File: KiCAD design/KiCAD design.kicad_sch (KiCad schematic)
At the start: 3 parts, among them U101 NUCLEO64-F411RE

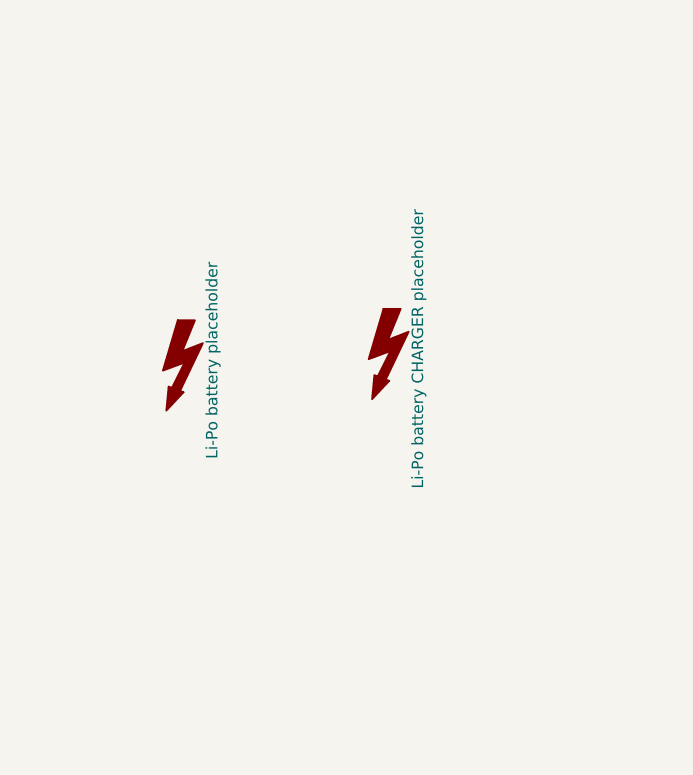
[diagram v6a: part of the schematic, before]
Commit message: added PurchaseLoc and Price to most of the main components, leds, resistors, capacitors, switch, bluetooth missing
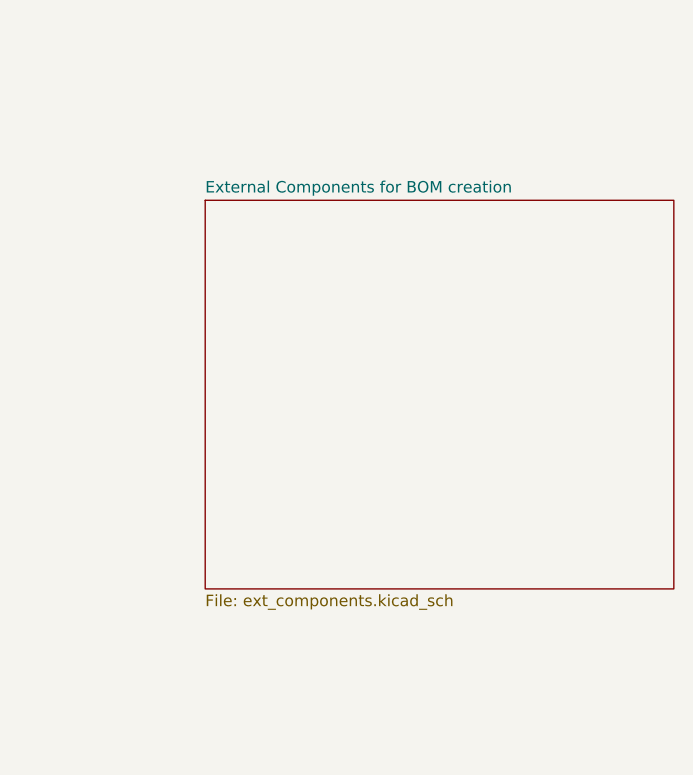
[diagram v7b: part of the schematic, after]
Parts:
- removed LiPo_bat401: Li-Po battery placeholder, symbol Graphic:SYM_Flash_Large
- removed LiPo_charger401: Li-Po battery CHARGER placeholder, symbol Graphic:SYM_Flash_Large
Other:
- added sheet External Components for BOM creation (ext_components.kicad_sch)
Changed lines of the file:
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@@
     (stroke (width 0) (type default) (color 0 0 0 0))
-  )
-  (symbol (lib_id "Graphic:SYM_Flash_Large") (at 207.01 127 0) (unit 1)
-    (in_bom yes) (on_board yes) (fields_autoplaced)
-    (property "Reference" "LiPo_bat401" (id 0) (at 203.2 127 90)
-      (effects (font (size 1.27 1.27)) hide)
-    )
-    (property "Value" "Li-Po battery placeholder" (id 1) (at 210.312 127 90))
-    (property "Footprint" "" (id 2) (at 206.756 129.286 0)
-      (effects (font (size 1.27 1.27)) hide)
-    )
-    (property "Datasheet" "~" (id 3) (at 217.17 129.54 0)
-      (effects (font (size 1.27 1.27)) hide)
-    )
-    (property "PurchaseLoc" "https://hobbyking.com/en_us/zippy-compact-1800mah-3s-25c-lipo-pack.html" (id 4) (at 207.01 127 90)
-      (effects (font (size 1.27 1.27)) hide)
-    )
-    (property "Price" "13.42" (id 5) (at 207.01 127 90)
-      (effects (font (size 1.27 1.27)) hide)
-    )
-  )
-  (symbol (lib_id "Graphic:SYM_Flash_Large") (at 229.87 125.73 0) (unit 1)
-    (in_bom yes) (on_board yes) (fields_autoplaced)
-    (property "Reference" "LiPo_charger401" (id 0) (at 226.06 125.73 90)
-      (effects (font (size 1.27 1.27)) hide)
-    )
-    (property "Value" "Li-Po battery CHARGER placeholder" (id 1) (at 233.172 125.73 90))
-    (property "Footprint" "" (id 2) (at 229.616 128.016 0)
-      (effects (font (size 1.27 1.27)) hide)
-    )
-    (property "Datasheet" "~" (id 3) (at 240.03 128.27 0)
-      (effects (font (size 1.27 1.27)) hide)
-    )
-    (property "PurchaseLoc" "https://hobbyking.com/en_us/turnigy-e3-compact-2s-3s-lipo-charger-100-240v-eu-plug.html" (id 4) (at 229.87 125.73 90)
-      (effects (font (size 1.27 1.27)) hide)
-    )
-    (property "Price" "14.39" (id 5) (at 229.87 125.73 90)
-      (effects (font (size 1.27 1.27)) hide)
-    )
   )
   (symbol (lib_id "MCU_Module:NUCLEO64-F411RE") (at 93.98 149.86 90) (unit 1)
@@
     )
   )
+  (sheet (at 209.55 109.22) (size 52.07 43.18) (fields_autoplaced)
+    (stroke (width 0.1524) (type solid) (color 0 0 0 0))
+    (fill (color 0 0 0 0.0000))
+    (property "Sheet name" "External Components for BOM creation" (id 0) (at 209.55 108.5084 0)
+      (effects (font (size 1.27 1.27)) (justify left bottom))
+    )
+    (property "Sheet file" "ext_components.kicad_sch" (id 1) (at 209.55 152.9846 0)
+      (effects (font (size 1.27 1.27)) (justify left top))
+    )
+  )
   (sheet_instances
     (path "/" (page "1"))
@@
     (path "/465a2d22-51a7-48d6-b1e0-fc75f581e914" (page "3"))
     (path "/3203fe18-fa26-4a56-94ee-1c822c5de1df" (page "4"))
+    (path "/84eed88b-177a-45c5-a159-b80e42fc88fa" (page "5"))
   )
   (symbol_instances
@@
       (reference "#PWR0403") (unit 1) (value "GND") (footprint "")
     )
+    (path "/84eed88b-177a-45c5-a159-b80e42fc88fa/e609e455-2f92-47cd-a338-cdee205ff5a8"
+      (reference "Bluetooth") (unit 1) (value "HC-05") (footprint "")
+    )
     (path "/465a2d22-51a7-48d6-b1e0-fc75f581e914/661a7e05-4c89-4c14-ad6b-8ac48096fd6e"
       (reference "C301") (unit 1) (value "10uF") (footprint "Capacitor_SMD:C_0603_1608Metric_Pad1.08x0.95mm_HandSolder")
@@
       (reference "J208") (unit 1) (value "JST SENS TOF 1") (footprint "Connector_JST:JST_XH_B6B-XH-A_1x06_P2.50mm_Vertical")
     )
-    (path "/11dd6d81-7255-48cc-8812-0f9f86181d16"
-      (reference "LiPo_bat401") (unit 1) (value "Li-Po battery placeholder") (footprint "")
-    )
-    (path "/300626cb-8874-43dc-8300-c3f8e2249cd7"
-      (reference "LiPo_charger401") (unit 1) (value "Li-Po battery CHARGER placeholder") (footprint "")
+    (path "/84eed88b-177a-45c5-a159-b80e42fc88fa/0329014d-46ad-4dfa-8935-5abae3a17d71"
+      (reference "LiPo_bat?") (unit 1) (value "Li-Po battery placeholder") (footprint "")
+    )
+    (path "/84eed88b-177a-45c5-a159-b80e42fc88fa/09caa74d-e3f7-4a3b-b30b-4c0c21f50184"
+      (reference "LiPo_charger?") (unit 1) (value "Li-Po battery CHARGER placeholder") (footprint "")
     )
     (path "/3203fe18-fa26-4a56-94ee-1c822c5de1df/babb38ec-e470-4f2b-ac32-e46727abe3d3"
@@
       (reference "SW301") (unit 1) (value "~") (footprint "composants_projet_footprint:1A11-NF5STSE-B")
     )
+    (path "/84eed88b-177a-45c5-a159-b80e42fc88fa/1effef2d-bafc-46de-9853-a1755d0a3819"
+      (reference "TOF1") (unit 1) (value "SEN0245") (footprint "")
+    )
+    (path "/84eed88b-177a-45c5-a159-b80e42fc88fa/5ccb8a2d-2973-4981-a068-a4deaf76301f"
+      (reference "TOF2") (unit 1) (value "SEN0245") (footprint "")
+    )
     (path "/53ab80cb-680d-47b5-9042-b10ff93ac434"
